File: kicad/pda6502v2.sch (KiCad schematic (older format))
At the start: 87 parts, among them J1 GPIO1, J2 GPIO2, J3 UART, J4 Screw_Terminal_01x02, J5 Conn_02x04_Odd_Even, J6 ICSP, J7 SPI, J8 FPGA_EXT, J9 SID, SW1 SW_Push, SW2 SW_Push, U1 W65C02SxP, U10 LT3030, U11 SC28L92A1B, U2 W65C22SxP, U3 W65C22SxP, U4 DS1818, U5 AS6C4008-55PCN, U6 ARMSID, U7 AT25M01, U8 ICE40HX4K-TQ144, U9 TLV1117-33, X1 8 MHz, X2 3.6864 MHz

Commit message: Lots of routing. Nearly done, but getting tight.
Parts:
- renumbered U3 to U2, U2 to U3
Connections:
- net A0: now also U5.5 (A7); no longer U5.12 (A0)
- net A1: now also U5.6 (A6); no longer U5.11 (A1)
- net A2: now also U5.7 (A5); no longer U5.10 (A2)
- net A3: now also U5.8 (A4); no longer U5.9 (A3)
- net A4: now also U5.9 (A3); no longer U5.8 (A4)
- net A5: now also U5.10 (A2); no longer U5.7 (A5)
- net A6: now also U5.11 (A1); no longer U5.6 (A6)
- net A7: now also U5.12 (A0); no longer U5.5 (A7)
- net D3: now also U5.21 (Q7); no longer U5.17 (Q3)
- net D4: now also U5.20 (Q6); no longer U5.18 (Q4)
- net D6: now also U5.18 (Q4); no longer U5.20 (Q6)
- net D7: now also U5.17 (Q3); no longer U5.21 (Q7)
- net RESET: now also U8.16 (IOL_10B); no longer U8.22 (IOL_14B)
- net SID_IN: now also J9.6 (Pin_6); no longer J9.5 (Pin_5)
- net SID_OUT: now also J9.5 (Pin_5); no longer J9.4 (Pin_4)
- net SID_X: now also J9.4 (Pin_4); no longer J9.3 (Pin_3)
- net SID_Y: now also J9.3 (Pin_3); no longer J9.6 (Pin_6)
- net SID_~CS: now also U8.12 (IOL_8B); no longer U8.24 (IOL_17B)
- net ~RESET: now also U8.17 (IOL_12A); no longer U8.23 (IOL_17A)
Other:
- moved on the sheet: J9
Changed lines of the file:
@@
 	4900 1100 5050 1100
 Text Label 4950 1800 0    50   ~ 0
-D7
+D3
 Text Label 4950 1700 0    50   ~ 0
-D6
+D4
 Text Label 4950 1600 0    50   ~ 0
 D5
 Text Label 4950 1500 0    50   ~ 0
-D4
+D6
 Text Label 4950 1400 0    50   ~ 0
-D3
+D7
 Text Label 4950 1300 0    50   ~ 0
 D2
@@
 $EndComp
 Text Label 3700 1100 0    50   ~ 0
-A0
+A7
 Text Label 3700 1200 0    50   ~ 0
-A1
+A6
 Text Label 3700 1300 0    50   ~ 0
-A2
+A5
 Text Label 3700 1400 0    50   ~ 0
-A3
-Text Label 3700 1500 0    50   ~ 0
 A4
+Text Label 3700 1500 0    50   ~ 0
+A3
 Text Label 3700 1600 0    50   ~ 0
-A5
+A2
 Text Label 3700 1700 0    50   ~ 0
-A6
+A1
 Text Label 3700 1800 0    50   ~ 0
-A7
+A0
 Text Label 3700 1900 0    50   ~ 0
 A8
@@
 Text Label 14750 5450 2    50   ~ 0
 CLOCKSRC
-Text Label 14750 5650 2    50   ~ 0
+Text Label 14750 5050 2    50   ~ 0
 RESET
-Text Label 14750 5750 2    50   ~ 0
+Text Label 14750 5150 2    50   ~ 0
 ~RESET
 Text Label 14750 4150 2    50   ~ 0
@@
 Wire Wire Line
 	4550 9150 4550 9250
-$Comp
-L pda6502v2:W65C22SxP U2
-U 1 1 6244272B
-P 1900 9250
-F 0 "U2" H 1900 10881 50  0000 C CNN
-F 1 "W65C22SxP" H 1900 10790 50  0000 C CIB
-F 2 "Package_DIP:DIP-40_W15.24mm" H 1900 9400 50  0001 C CNN
-F 3 "http://www.westerndesigncenter.com/wdc/documentation/w65c22.pdf" H 1900 9400 50  0001 C CNN
-	1    1900 9250
-	1    0    0    -1
-$EndComp
 Wire Wire Line
 	2500 8950 2900 8950
@@
 	8550 9150 8550 9250
 $Comp
-L pda6502v2:W65C22SxP U3
+L pda6502v2:W65C22SxP U2
 U 1 1 62BC495B
 P 5900 9250
-F 0 "U3" H 5900 10881 50  0000 C CNN
+F 0 "U2" H 5900 10881 50  0000 C CNN
 F 1 "W65C22SxP" H 5900 10790 50  0000 C CIB
 F 2 "Package_DIP:DIP-40_W15.24mm" H 5900 9400 50  0001 C CNN
@@
 $EndComp
 Wire Wire Line
-	9100 5250 9100 5050
+	9100 5550 9100 5350
 Wire Wire Line
-	9100 5050 9200 5050
+	9100 5350 9200 5350
 $Comp
 L Connector_Generic:Conn_02x04_Odd_Even J9
 U 1 1 67B17C61
-P 8800 5350
-F 0 "J9" H 8850 5667 50  0000 C CNN
-F 1 "SID" H 8850 5576 50  0000 C CNN
-F 2 "Connector_PinHeader_2.54mm:PinHeader_2x04_P2.54mm_Vertical" H 8800 5350 50  0001 C CNN
-F 3 "~" H 8800 5350 50  0001 C CNN
-	1    8800 5350
-	1    0    0    -1
+P 8900 5750
+F 0 "J9" H 8950 6067 50  0000 C CNN
+F 1 "SID" H 8950 5976 50  0000 C CNN
+F 2 "Connector_PinHeader_2.54mm:PinHeader_2x04_P2.54mm_Vertical" H 8900 5750 50  0001 C CNN
+F 3 "~" H 8900 5750 50  0001 C CNN
+	1    8900 5750
+	-1   0    0    1
 $EndComp
 $Comp
 L power:+5V #PWR0119
 U 1 1 678A04B9
-P 8550 5200
-F 0 "#PWR0119" H 8550 5050 50  0001 C CNN
-F 1 "+5V" H 8565 5373 50  0000 C CNN
-F 2 "" H 8550 5200 50  0001 C CNN
-F 3 "" H 8550 5200 50  0001 C CNN
-	1    8550 5200
+P 8550 5500
+F 0 "#PWR0119" H 8550 5350 50  0001 C CNN
+F 1 "+5V" H 8565 5673 50  0000 C CNN
+F 2 "" H 8550 5500 50  0001 C CNN
+F 3 "" H 8550 5500 50  0001 C CNN
+	1    8550 5500
 	1    0    0    -1
 $EndComp
@@
 L power:GND #PWR0120
 U 1 1 688A6E95
-P 9200 5050
-F 0 "#PWR0120" H 9200 4800 50  0001 C CNN
-F 1 "GND" H 9205 4877 50  0000 C CNN
-F 2 "" H 9200 5050 50  0001 C CNN
-F 3 "" H 9200 5050 50  0001 C CNN
-	1    9200 5050
+P 9200 5350
+F 0 "#PWR0120" H 9200 5100 50  0001 C CNN
+F 1 "GND" H 9205 5177 50  0000 C CNN
+F 2 "" H 9200 5350 50  0001 C CNN
+F 3 "" H 9200 5350 50  0001 C CNN
+	1    9200 5350
 	1    0    0    -1
 $EndComp
-Text Label 9100 5350 0    50   ~ 0
+Text Label 9100 5650 0    50   ~ 0
 SID_OUT
-Text Label 8600 5450 2    50   ~ 0
+Text Label 8600 5650 2    50   ~ 0
 SID_IN
-Text Label 8600 5350 2    50   ~ 0
+Text Label 8600 5750 2    50   ~ 0
 SID_X
-Text Label 9100 5450 0    50   ~ 0
+Text Label 9100 5750 0    50   ~ 0
 SID_Y
 Wire Wire Line
@@
 Connection ~ 8050 5950
 Wire Wire Line
-	8050 5950 8300 5950
+	8050 5950 8250 5950
 Wire Wire Line
 	6750 4650 6800 4650
 Wire Wire Line
 	6750 4750 6800 4750
-Text Label 14750 5850 2    50   ~ 0
+Text Label 14750 4850 2    50   ~ 0
 SID_~CS
 $Comp
@@
 L power:+5V #PWR0121
 U 1 1 6AC709BE
-P 9200 5700
-F 0 "#PWR0121" H 9200 5550 50  0001 C CNN
-F 1 "+5V" H 9215 5873 50  0000 C CNN
-F 2 "" H 9200 5700 50  0001 C CNN
-F 3 "" H 9200 5700 50  0001 C CNN
-	1    9200 5700
+P 9200 6000
+F 0 "#PWR0121" H 9200 5850 50  0001 C CNN
+F 1 "+5V" H 9215 6173 50  0000 C CNN
+F 2 "" H 9200 6000 50  0001 C CNN
+F 3 "" H 9200 6000 50  0001 C CNN
+	1    9200 6000
 	1    0    0    -1
 $EndComp
 Wire Wire Line
-	9100 5550 9100 5700
+	9100 5850 9100 6000
 Wire Wire Line
-	9100 5700 9200 5700
+	9100 6000 9200 6000
 $Comp
 L power:GND #PWR0122
 U 1 1 6AD630D8
-P 8550 5550
-F 0 "#PWR0122" H 8550 5300 50  0001 C CNN
-F 1 "GND" H 8555 5377 50  0000 C CNN
-F 2 "" H 8550 5550 50  0001 C CNN
-F 3 "" H 8550 5550 50  0001 C CNN
-	1    8550 5550
+P 8550 5850
+F 0 "#PWR0122" H 8550 5600 50  0001 C CNN
+F 1 "GND" H 8555 5677 50  0000 C CNN
+F 2 "" H 8550 5850 50  0001 C CNN
+F 3 "" H 8550 5850 50  0001 C CNN
+	1    8550 5850
 	1    0    0    -1
 $EndComp
 Wire Wire Line
-	8600 5550 8550 5550
+	8600 5850 8550 5850
 Wire Wire Line
-	9450 4950 9450 5350
+	9450 4950 9450 5650
 Wire Wire Line
-	9450 5350 9100 5350
+	9450 5650 9100 5650
 Wire Wire Line
 	8250 4950 9450 4950
 Wire Wire Line
-	8250 5450 8600 5450
-Wire Wire Line
-	8300 5350 8600 5350
-Wire Wire Line
-	8300 5350 8300 5950
-Wire Wire Line
-	8600 5250 8550 5250
-Wire Wire Line
-	8550 5250 8550 5200
+	8600 5550 8550 5550
 Wire Wire Line
-	8050 6450 8400 6450
+	8550 5550 8550 5500
 Wire Wire Line
-	8400 6450 8400 5800
+	8050 6450 9450 6450
 Connection ~ 8050 6450
 Wire Wire Line
-	9100 5450 9450 5450
-Wire Wire Line
-	8400 5800 9450 5800
-Wire Wire Line
-	9450 5800 9450 5450
+	9100 5750 9450 5750
 Wire Wire Line
 	10050 5750 10250 5750
@@
 NoConn ~ 11750 6350
 NoConn ~ 13250 3950
-NoConn ~ 14750 4850
-NoConn ~ 14750 5050
-NoConn ~ 14750 5150
+NoConn ~ 14750 5650
+NoConn ~ 14750 5750
 NoConn ~ 14750 5250
 NoConn ~ 14750 5550
@@
 Wire Wire Line
 	8000 1300 8000 1750
-Wire Bus Line
-	6600 6250 6600 7000
+Text Label 12950 7850 2    50   ~ 0
+VCC_FLASH
+$Comp
+L pda6502v2:W65C22SxP U3
+U 1 1 6244272B
+P 1900 9250
+F 0 "U3" H 1900 10881 50  0000 C CNN
+F 1 "W65C22SxP" H 1900 10790 50  0000 C CIB
+F 2 "Package_DIP:DIP-40_W15.24mm" H 1900 9400 50  0001 C CNN
+F 3 "http://www.westerndesigncenter.com/wdc/documentation/w65c22.pdf" H 1900 9400 50  0001 C CNN
+	1    1900 9250
+	1    0    0    -1
+$EndComp
+NoConn ~ 14750 5850
+Wire Wire Line
+	9450 5750 9450 6450
+Wire Wire Line
+	8250 5450 8250 5650
+Wire Wire Line
+	8250 5650 8600 5650
+Wire Wire Line
+	8250 5950 8250 5750
+Wire Wire Line
+	8250 5750 8600 5750
 Wire Bus Line
 	6500 5450 6500 5900
 Wire Bus Line
-	5100 9750 5100 10500
-Wire Bus Line
 	4900 9050 4900 9400
 Wire Bus Line
-	14250 6050 14250 6850
+	1650 4700 1650 5050
 Wire Bus Line
-	9250 10150 9250 10950
+	900  9050 900  9400
 Wire Bus Line
-	9850 5700 9850 6450
+	6600 6250 6600 7000
 Wire Bus Line
-	9950 3750 9950 5650
+	5100 9750 5100 10500
 Wire Bus Line
-	1650 6200 1650 6950
+	14250 6050 14250 6850
 Wire Bus Line
-	1650 4700 1650 5050
+	9250 10150 9250 10950
 Wire Bus Line
-	2750 1000 2750 2550
+	9850 5700 9850 6450
 Wire Bus Line
-	3600 1200 3600 3100
+	1650 6200 1650 6950
 Wire Bus Line
 	5150 950  5150 1700
@@
 	1100 9750 1100 10500
 Wire Bus Line
-	900  9050 900  9400
-Wire Bus Line
 	2750 2950 2750 3700
-Text Label 12950 7850 2    50   ~ 0
-VCC_FLASH
+Wire Bus Line
+	2750 1000 2750 2550
+Wire Bus Line
+	3600 1200 3600 3100
+Wire Bus Line
+	9950 3750 9950 5650
 $EndSCHEMATC

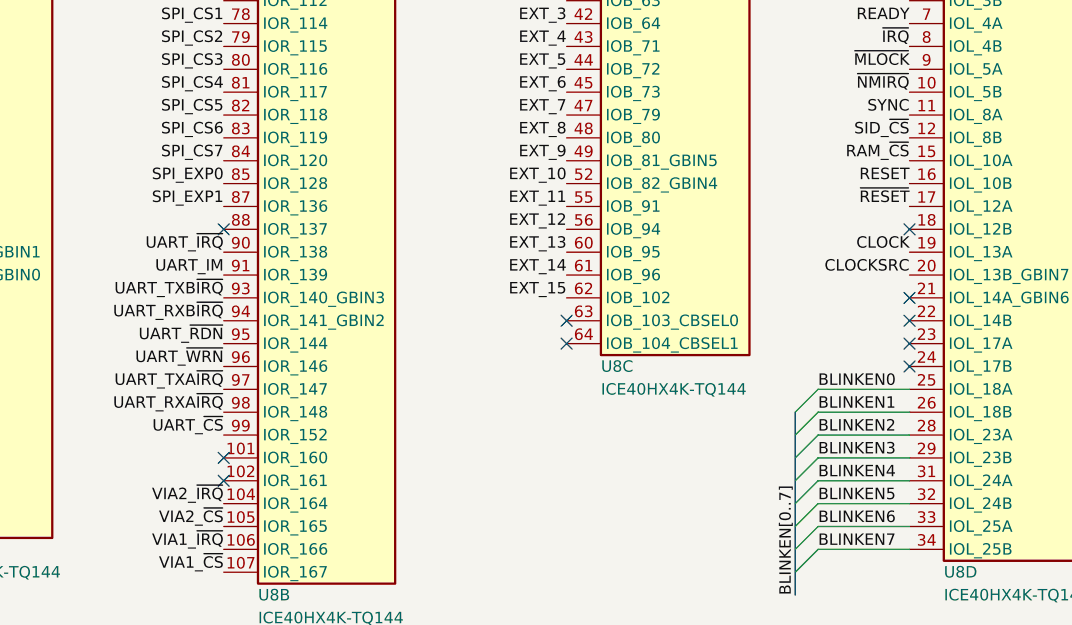
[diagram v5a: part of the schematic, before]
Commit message: More routing. D[0..7] etc.
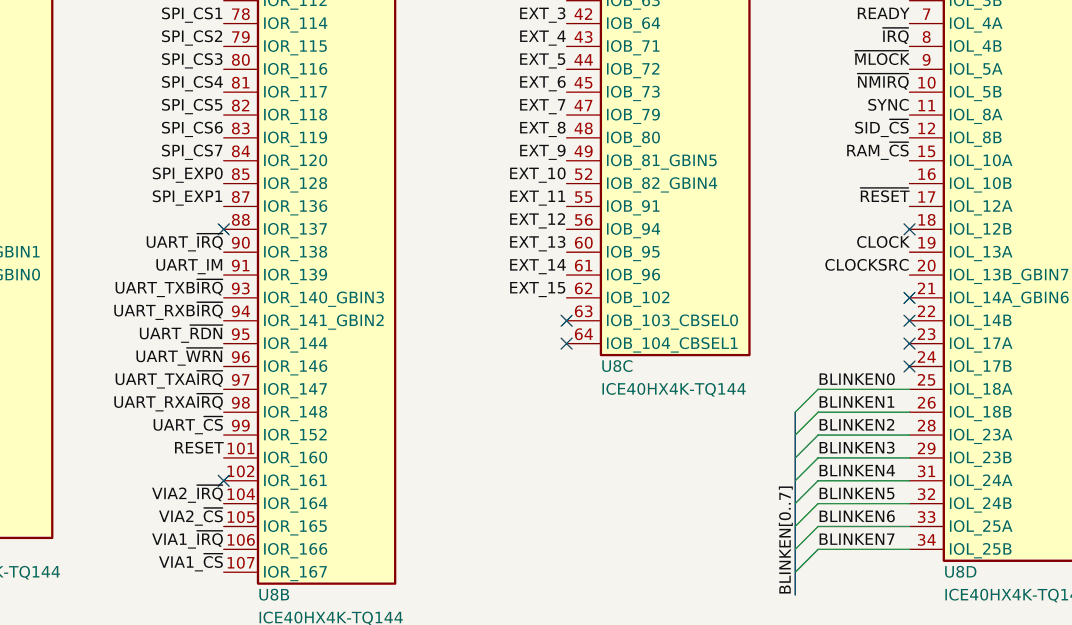
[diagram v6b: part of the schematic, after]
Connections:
- net RESET: now also U8.101 (IOR_160); no longer U8.16 (IOL_10B)
- no-connect marks 27 -> 26
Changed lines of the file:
@@
 Text Label 14750 5450 2    50   ~ 0
 CLOCKSRC
-Text Label 14750 5050 2    50   ~ 0
+Text Label 11750 6250 2    50   ~ 0
 RESET
 Text Label 14750 5150 2    50   ~ 0
@@
 EXT_13
 NoConn ~ 11750 5250
-NoConn ~ 11750 6250
 NoConn ~ 11750 6350
 NoConn ~ 13250 3950

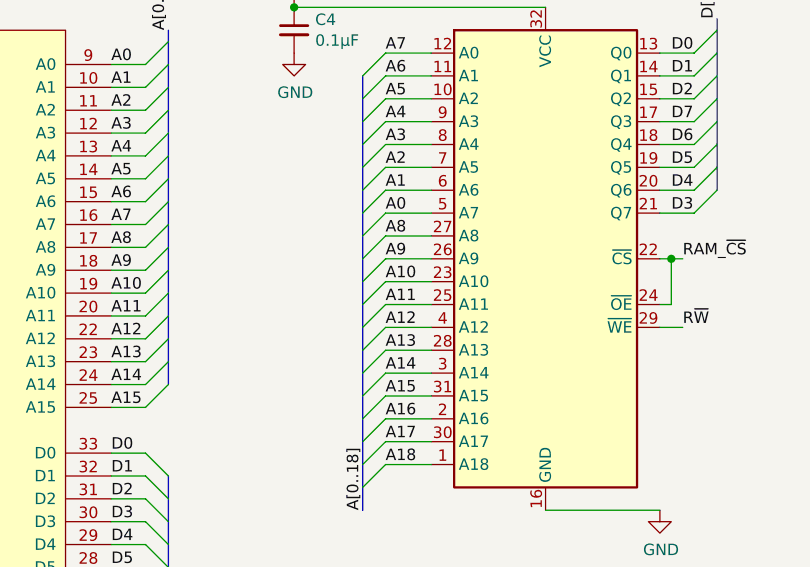
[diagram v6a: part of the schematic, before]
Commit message: PCB 100% routed
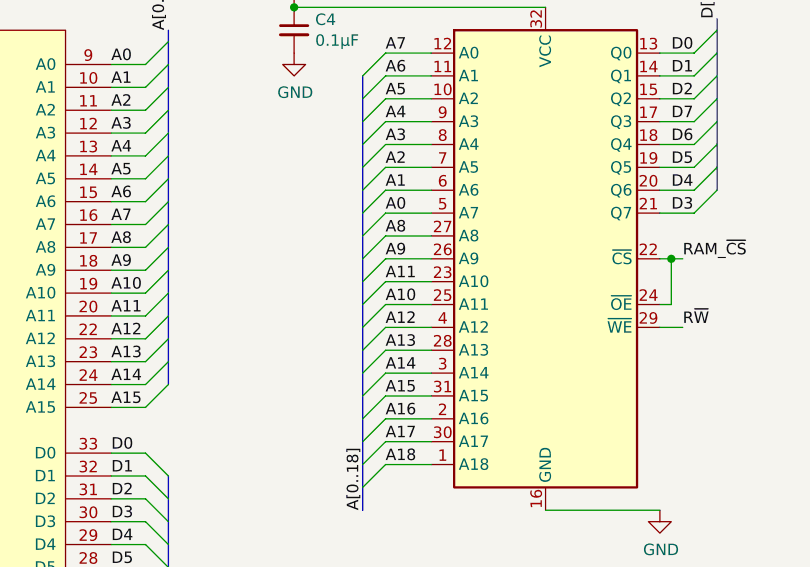
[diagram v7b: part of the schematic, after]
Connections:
- net A10: now also U5.25 (A11); no longer U5.23 (A10)
- net A11: now also U5.23 (A10); no longer U5.25 (A11)
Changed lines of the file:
@@
 Text Label 3700 2000 0    50   ~ 0
 A9
+Text Label 3700 2200 0    50   ~ 0
+A10
 Text Label 3700 2100 0    50   ~ 0
-A10
-Text Label 3700 2200 0    50   ~ 0
 A11
 Text Label 3700 2300 0    50   ~ 0

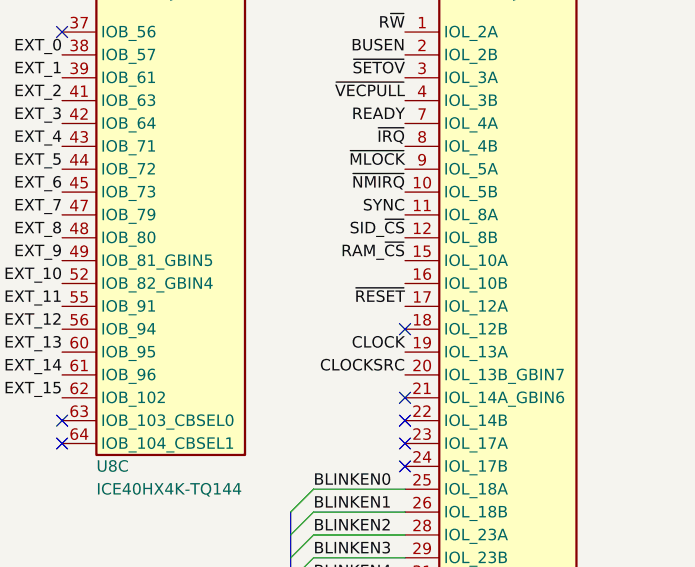
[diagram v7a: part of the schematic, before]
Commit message: PA initials and "v2" on PCB, plus some tweaks.
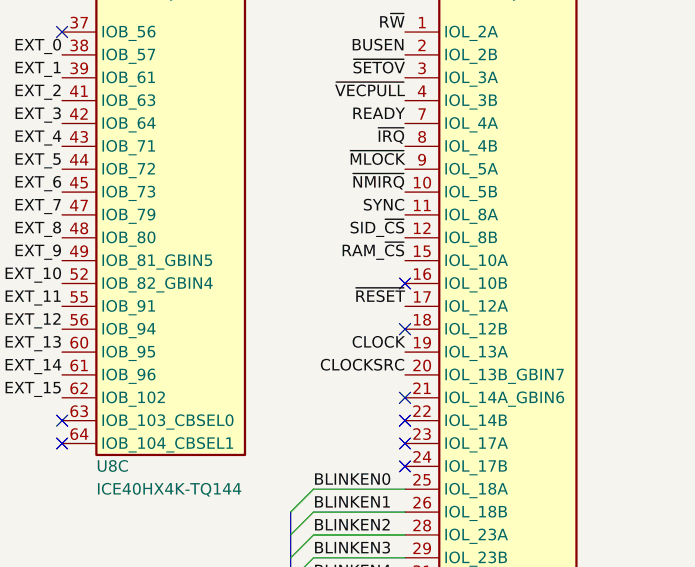
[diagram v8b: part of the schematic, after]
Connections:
- no-connect marks 26 -> 27
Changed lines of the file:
@@
 Wire Wire Line
 	8250 5750 8600 5750
+NoConn ~ 14750 5050
 Wire Bus Line
 	6500 5450 6500 5900
